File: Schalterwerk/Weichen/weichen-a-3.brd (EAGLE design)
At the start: 100 x 80 mm, 24 parts, among them Q1 P-MOSFET, Q2 P-MOSFET, X1 PHNX_4P_508CONN_1017493, X3 IO-HAT, X4 RJ45-JACK, X5 PHNX_4P_350CONN_1984989_PXC, X6 PHNX_4P_350CONN_1984989_PXC

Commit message: Completes copy-paste of the layout of the conneectors to the schalterwerk.
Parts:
- added H1, H2, H3, H4: MOUNT-HOLE3.3, holes:3,3
- moved X4 222.4 mm to (95.2, 40.0), turned to 90 degrees
- moved X6 173.7 mm to (95.2, 15.2), turned to 90 degrees
- moved X5 144.5 mm to (95.2, 54.6), turned to 90 degrees
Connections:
- net NX41: now also X5.4; no longer X5.1
- net NX42: now also X5.3; no longer X5.2
- net NX43: now also X5.2; no longer X5.3
- net NX44: now also X6.4; no longer X6.1
- net NX45: now also X6.3; no longer X6.2
- net NX46: now also X5.1; no longer X5.4
- net NX47: now also X6.2; no longer X6.3
- net NX48: now also X6.1; no longer X6.4
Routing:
- net NX41: track 0.00 -> 64.1 mm, vias 0 -> 3
- net NX48: track 0.00 -> 56.9 mm, vias 0 -> 1
- net NX47: track 0.00 -> 53.0 mm, vias 0 -> 1
- net NX42: track 0.00 -> 52.3 mm, vias 0 -> 1
- net NX43: track 0.00 -> 49.2 mm, vias 0 -> 3
- net NX45: track 0.00 -> 44.2 mm, vias 0 -> 1
- net NX46: track 0.00 -> 42.3 mm, vias 0 -> 1
- net NX44: track 0.00 -> 37.7 mm, vias 0 -> 1
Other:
- board size 100 x 80 mm -> 100.3 x 80 mm
- board text added: "CH1 schalt"
- board text added: "CH2 schalt"
- board text added: "CH3 schalt"
- board text added: "CH4 schalt"
- board text added: "V+"

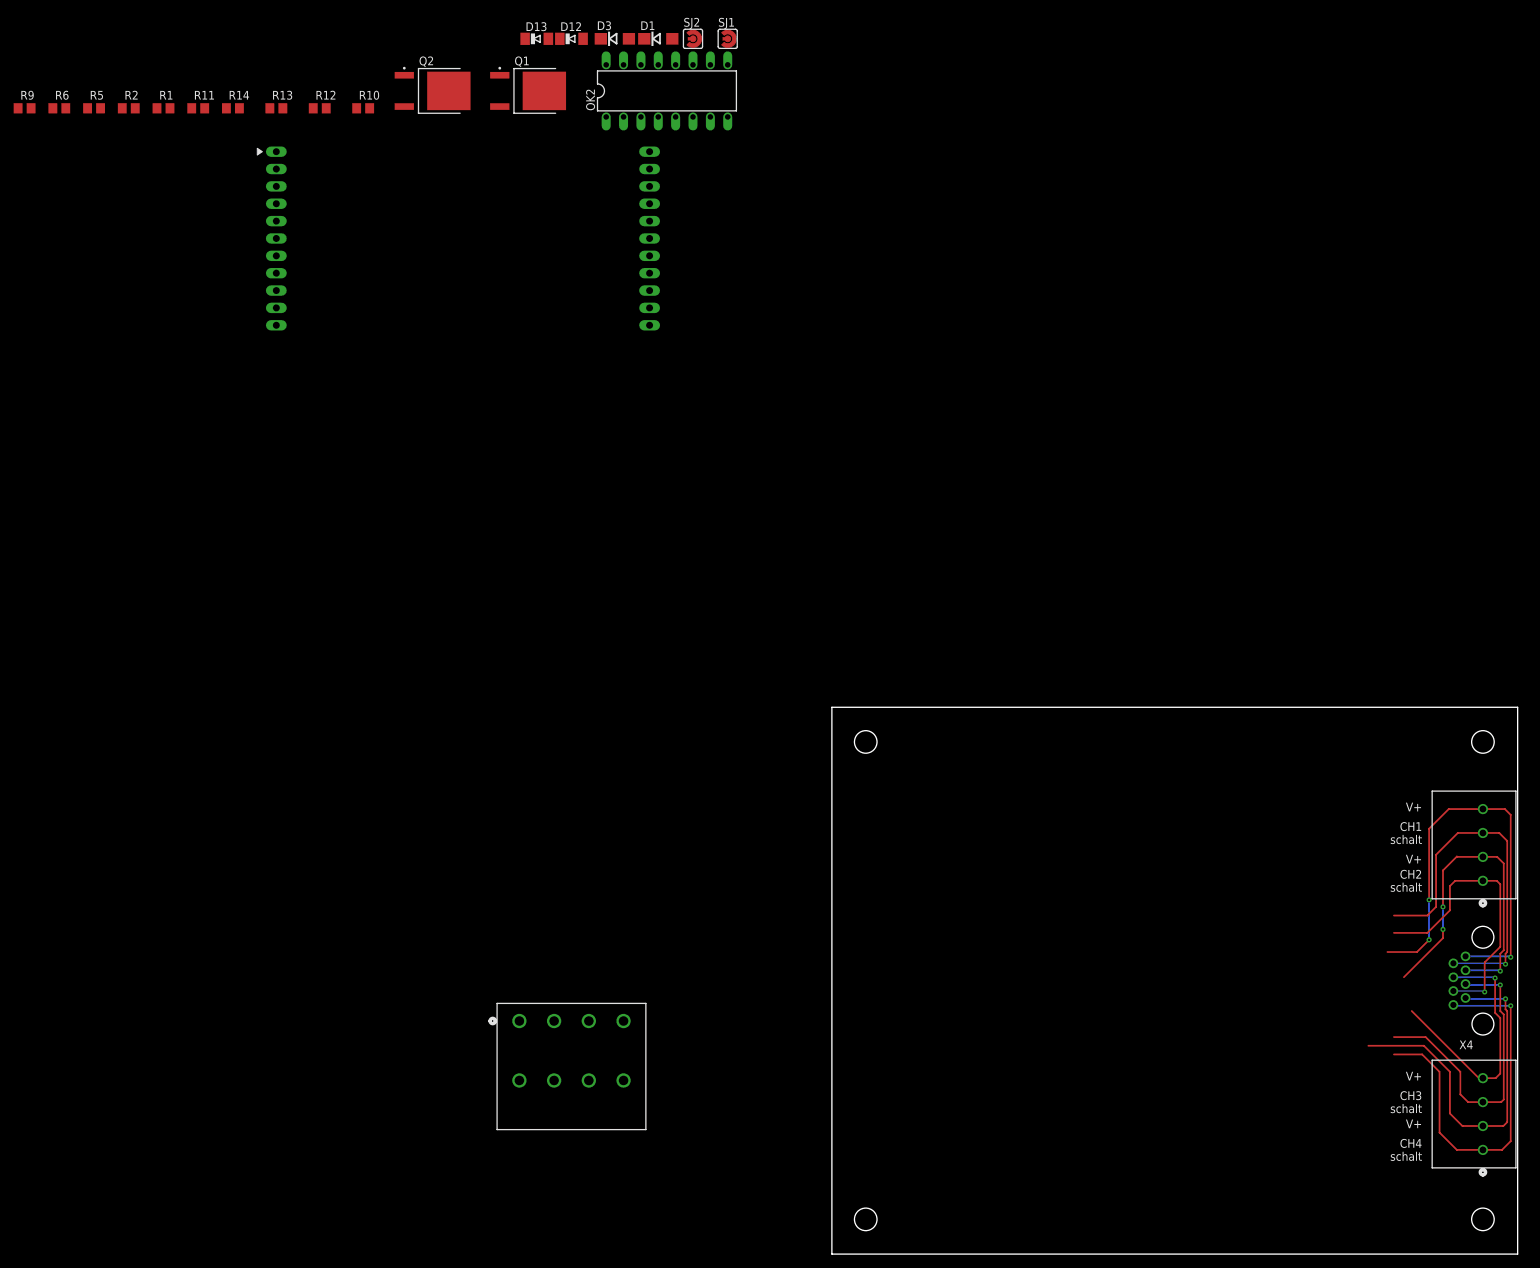
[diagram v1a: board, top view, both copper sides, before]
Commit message: Does much of the board layout. Switches the pins on the connector to the schalterwerk so that it is in the order of L1 .. L4.
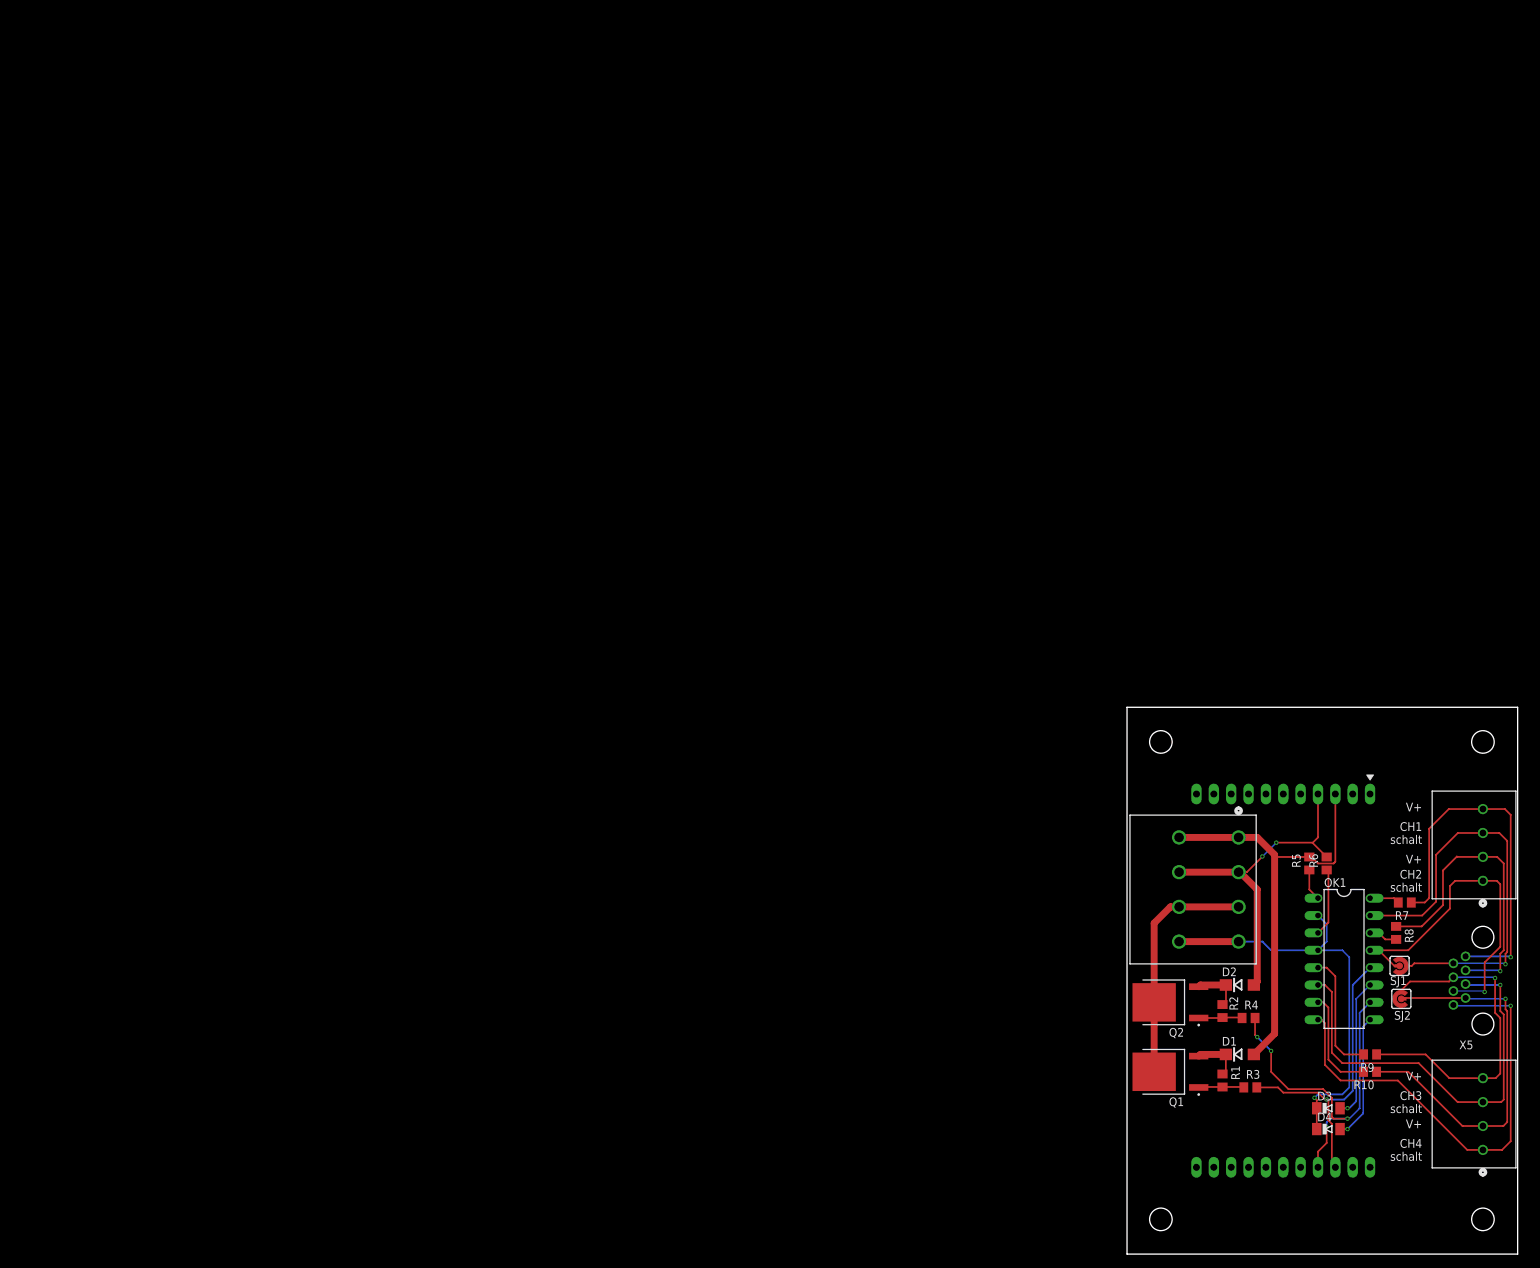
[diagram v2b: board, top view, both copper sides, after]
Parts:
- removed D12, D13: (no value), diode:MINIMELF
- removed OK2: PC847, optocoupler:DIL16
- removed R11, R12: 100, rcl:R0805
- removed R13, R14: 1k5, rcl:R0805
- removed X6: PHNX_4P_350CONN_1984989_PXC, eagleparts:PHNX_4P_350
- added D2: (no value), diode:DO214AC
- added D4: (no value), diode:MINIMELF
- added OK1: PC847, optocoupler:DIL16
- added R3, R4: 5k, rcl:R0805
- added R7, R8: 100, rcl:R0805
- added X2: IO-HAT, eagleparts:IOBOARD
- D3: device diode:DO214AC -> diode:MINIMELF
- R10, R9: value 5k -> 1k5
- X3: value IO-HAT -> PHNX_4P_350CONN_1984989_PXC; device eagleparts:IOBOARD -> eagleparts:PHNX_4P_350
- X4: value RJ45-JACK -> PHNX_4P_350CONN_1984989_PXC; device trainlib:RJ45-PULSE-E5J88 -> eagleparts:PHNX_4P_350
- X5: value PHNX_4P_350CONN_1984989_PXC -> RJ45-JACK; device eagleparts:PHNX_4P_350 -> trainlib:RJ45-PULSE-E5J88
- moved R9 240.7 mm to (78.7, 29.2), turned to 180 degrees
- moved R6 215.8 mm to (72.4, 57.1), turned to 90 degrees
- moved R1 210.3 mm to (57.1, 25.4), turned to 270 degrees
- moved R5 209.3 mm to (69.8, 57.1), turned to 90 degrees
- moved R2 207.5 mm to (57.1, 35.6), turned to 270 degrees
- moved X3 205.0 mm to (95.2, 54.6), turned to 90 degrees
- moved R10 203.9 mm to (78.7, 26.7), turned to 180 degrees
- moved D3 188.1 mm to (72.6, 21.3)
- moved SJ2 174.6 mm to (83.3, 37.3), turned to 180 degrees
- moved Q2 171.6 mm to (49.5, 36.8), turned to 180 degrees
- moved Q1 171.5 mm to (49.5, 26.7), turned to 180 degrees
- moved D1 171.2 mm to (59.7, 29.2)
- moved SJ1 167.5 mm to (83.1, 42.2)
- moved X1 83.8 mm to (50.8, 45.7), turned to 270 degrees
- moved H1 43.2 mm to (48.1, 74.9)
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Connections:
- net +12V: now also X2.P$1; no longer X3.P$1
- net 12V2: now also X2.P$22; no longer X3.P$22
- net GND: now also X2.P$11, X2.P$12, X2.P$2, X2.P$21; no longer X3.P$11, X3.P$12, X3.P$2, X3.P$21
- net L1: now also R5.2, X2.P$3; no longer R9.2, X3.P$3
- net L2: now also D2.A, R6.2, X1.3, X1.4, X2.P$4; no longer D3.A, R10.2, X1.5, X1.6, X3.P$4
- net L3: now also X1.5, X1.6; no longer X1.3, X1.4
- net L4: now also D3.C, D4.C, OK1.2, OK1.4; no longer D12.C, D13.C, OK2.2, OK2.4
- net N$1: now also D2.C; no longer D3.C
- net N$12: now also R4.1; no longer R6.1
- net N$15: now also OK1.12, R3.2, X2.P$20; no longer OK2.12, R5.2, X3.P$20
- net N$16: now also OK1.10, R4.2, X2.P$19; no longer OK2.10, R6.2, X3.P$19
- net N$17: now also D3.A, OK1.11; no longer D12.A, OK2.11
- net N$19: now also OK1.16, R7.2; no longer OK2.16, R11.2
- net N$2: now also OK1.1, R5.1; no longer OK2.1, R9.1
- net N$21: now also OK1.14, R8.2; no longer OK2.14, R12.2
- net N$22: now also D4.A, OK1.9; no longer D13.A, OK2.9
- net N$24: now also X2.P$18; no longer X3.P$18
- net N$25: now also X2.P$17; no longer X3.P$17
- net N$5: now also OK1.5, R9.2; no longer OK2.5, R13.2
- net N$7: now also OK1.3, R6.1; no longer OK2.3, R10.1
- net N$8: now also OK1.7, R10.2; no longer OK2.7, R14.2
- net N$9: now also R3.1; no longer R5.1
- net NX41: now also R7.1, X3.4, X5.1; no longer R11.1, X4.1, X5.4
- net NX42: now also OK1.15, X3.3, X5.2; no longer OK2.15, X4.2, X5.3
- net NX43: now also R8.1, X3.2, X5.3; no longer R12.1, X4.3, X5.2
- net NX44: now also R9.1, X5.4; no longer R13.1, X6.4
- net NX45: now also OK1.6, X4.3, X5.5; no longer OK2.6, X4.5, X6.3
- net NX46: now also OK1.13, X3.1, X5.6; no longer OK2.13, X4.6, X5.1
- net NX47: now also R10.1, X4.2, X5.7; no longer R14.1, X4.7, X6.2
- net NX48: now also OK1.8, X4.1, X5.8; no longer OK2.8, X4.8, X6.1
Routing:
- net L1: track 0.00 -> 64.9 mm
- net L4: track 0.00 -> 61.4 mm, vias 0 -> 1
- net N$16: track 0.00 -> 53.4 mm, vias 0 -> 4
- net L2: track 0.00 -> 49.6 mm, vias 0 -> 2
- net N$15: track 0.00 -> 44.8 mm, vias 0 -> 1
- net L3: track 0.00 -> 35.1 mm
- net N$17: track 0.00 -> 20.6 mm, vias 0 -> 1
- net N$22: track 0.00 -> 18.5 mm, vias 0 -> 1
- net N$5: track 0.00 -> 17.9 mm
- net NX45: track 44.2 -> 61.7 mm
- net N$8: track 0.00 -> 15.3 mm
- net NX44: track 37.7 -> 50.9 mm
- net NX48: track 56.9 -> 68.4 mm
- net NX41: track 64.1 -> 54.0 mm, vias 3 -> 1
- net NX42: track 52.3 -> 62.4 mm
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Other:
- board size 100.3 x 80 mm -> 57.1 x 80 mm

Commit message: Adds all display LEDs, completes layout.
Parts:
- added C1, C2: 500n25V, rcl:C0805
- added D10, D12, D6, D8: LEDHEADER, eagleparts:LEDHEADER
- added D11, D5, D7, D9: (no value), led:CHIPLED_0603
- added R11, R12, R13, R14, R17, R18: 5k, rcl:R0805
- added R15, R16: 10k, rcl:R0805
- moved R1 2.54 mm to (59.7, 25.4)
- moved R2 2.54 mm to (59.7, 35.6)
- moved R4 1.63 mm to (62.2, 35.6), turned to 90 degrees
- moved R3 1.44 mm to (62.2, 25.4), turned to 90 degrees
- moved Q1 0.76 mm to (50.3, 26.7)
- moved Q2 0.76 mm to (50.3, 36.8)
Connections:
- removed net N$15: OK1.12, R3.2, X2.P$20
- removed net N$16: OK1.10, R4.2, X2.P$19
- removed net N$9: Q1.1, R1.2, R3.1
- new net IST1: D10.C, D9.C, OK1.12, R3.2, X2.P$20
- new net IST2: D11.C, D12.C, OK1.10, R4.2, X2.P$19
- new net N$10: D8.A, R12.1
- new net N$11: D9.A, R15.1
- new net N$14: D10.A, R16.1
- new net N$18: D11.A, R17.1
- new net N$20: D12.A, R18.1
- new net N$23: C1.2, Q1.1, R1.2, R3.1
- new net N$3: D7.A, R11.1
- new net N$4: D5.A, R13.1
- new net N$6: D6.A, R14.1
- net L1: now also R13.2, R14.2
- net L2: now also R11.2, R12.2
- net L4: now also D5.C, D6.C, D7.C, D8.C
- net N$1: now also C2.1, R17.2, R18.2
- net N$12: now also C2.2
- net N$13: now also C1.1, R15.2, R16.2
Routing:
- net IST1: track 0.00 -> 92.7 mm, vias 0 -> 4
- net IST2: track 0.00 -> 92.0 mm, vias 0 -> 8
- net L4: track 61.4 -> 131.1 mm, vias 1 -> 2
- net N$1: track 7.26 -> 69.4 mm, vias 0 -> 6
- net L2: track 49.6 -> 111.7 mm
- net N$16: track 53.4 -> 0.00 mm, vias 4 -> 0
- net N$15: track 44.8 -> 0.00 mm, vias 1 -> 0
- net L1: track 64.9 -> 102.9 mm
- net N$13: track 7.14 -> 41.5 mm, vias 0 -> 6
- net N$23: track 0.00 -> 7.93 mm
- net N$9: track 6.65 -> 0.00 mm
- net N$6: track 0.00 -> 5.40 mm
- net N$3: track 0.00 -> 5.32 mm
- net N$4: track 0.00 -> 5.28 mm
- net N$20: track 0.00 -> 5.21 mm
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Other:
- board text added: "(c) Balazs Racz 20230601"
- board text added: "+"
- board text added: "-"
- board text added: "Ist"
- board text added: "Ist+ schalt"
- board text added: "Ist- schalt"
- board text added: "Masse"
- board text added: "Soll"
- board text added: "Soll + RM"
- board text added: "Soll - RM"
- board text removed: "CH1 schalt"
- board text removed: "CH2 schalt"
- board text removed: "CH3 schalt"
- board text removed: "CH4 schalt"

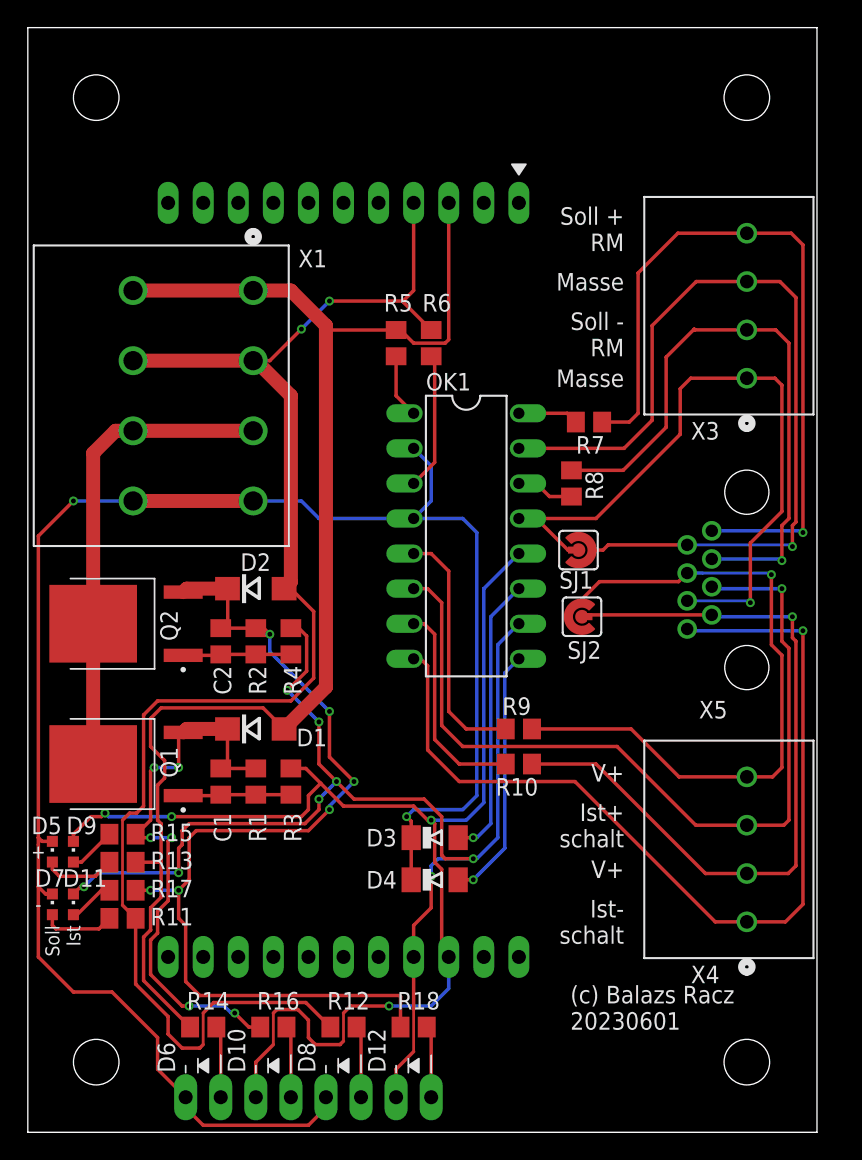
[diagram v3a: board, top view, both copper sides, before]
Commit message: Adds ports to connect adjacent boards. Adds ground pour.
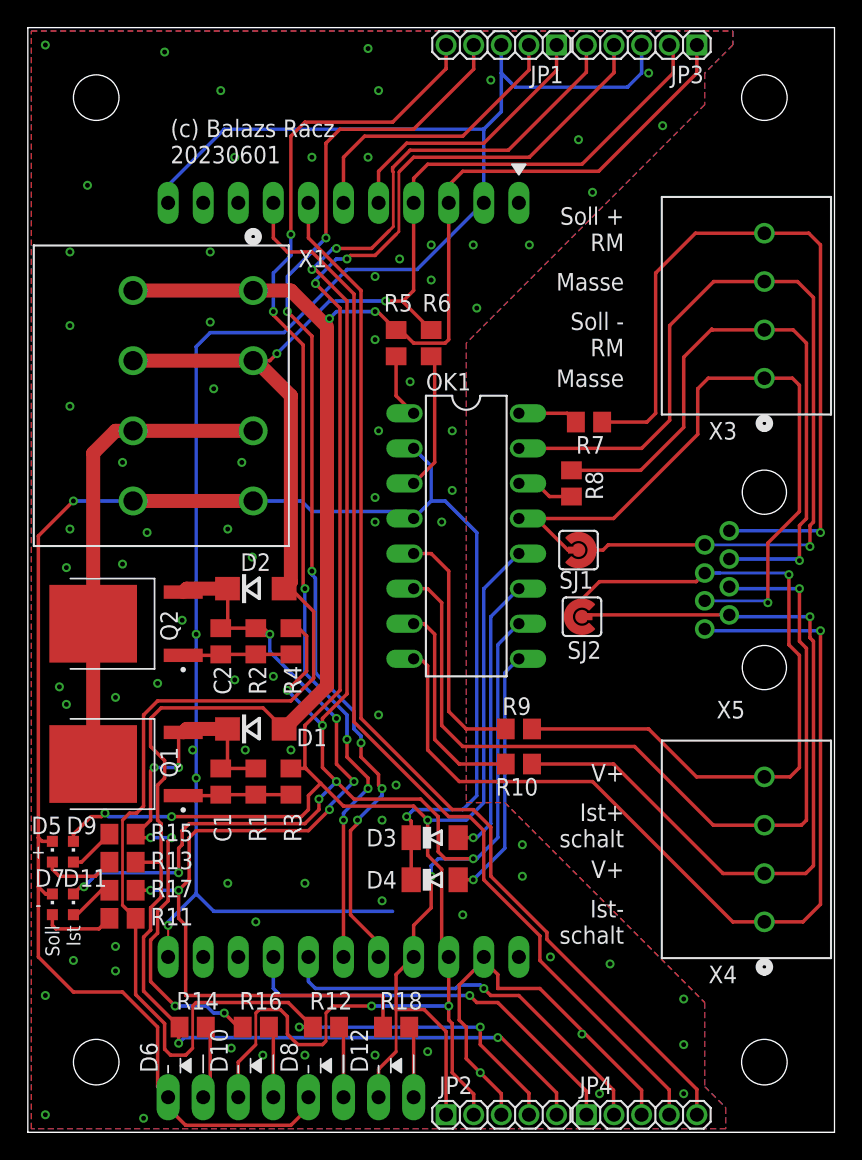
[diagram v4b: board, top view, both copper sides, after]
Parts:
- added JP1, JP2, JP3, JP4: (no value), pinhead:1_05X2MM
- moved D12 1.27 mm to (69.8, 2.54)
- moved D8 1.27 mm to (64.8, 2.54)
- moved R12 1.27 mm to (64.8, 7.62)
- moved R18 1.27 mm to (69.8, 7.62)
- moved D10 1.27 mm to (59.7, 2.54)
- moved D6 1.27 mm to (54.6, 2.54)
- moved R16 1.27 mm to (59.7, 7.62)
- moved H3 1.27 mm to (96.5, 5.08)
- moved H4 1.27 mm to (96.5, 74.9)
- moved X3 1.27 mm to (96.5, 54.6)
- moved X4 1.27 mm to (96.5, 15.2)
- moved X5 1.27 mm to (96.5, 40.0)
- moved R14 0.76 mm to (55.1, 7.62)
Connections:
- removed net N$24: X2.P$18
- removed net N$25: X2.P$17
- new net IN2: JP1.1, X2.P$5
- new net IN3: JP1.2, X2.P$6
- new net IN4: JP4.5, X2.P$7
- new net IN5: JP4.4, X2.P$8
- new net OUT2: JP1.4, X2.P$18
- new net OUT3: JP1.5, X2.P$17
- new net OUT4: JP4.2, X2.P$16
- new net OUT5: JP4.1, X2.P$15
- net GND: now also JP1.3, JP2.3, JP3.3, JP4.3
- net IST1: now also JP2.2, JP3.4
- net IST2: now also JP2.1, JP3.5
- net L1: now also JP2.5, JP3.1
- net L2: now also JP2.4, JP3.2
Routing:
- net GND: track 0.00 -> 166.9 mm, vias 0 -> 85
- net IST1: track 92.7 -> 173.0 mm, vias 4 -> 7
- net IN5: track 0.00 -> 79.8 mm
- net OUT2: track 0.00 -> 79.4 mm, vias 0 -> 6
- net IN4: track 0.00 -> 78.6 mm
- net OUT3: track 0.00 -> 78.5 mm, vias 0 -> 6
- net IST2: track 92.0 -> 168.0 mm, vias 8 -> 10
- net L1: track 102.9 -> 160.6 mm, vias 0 -> 4
- net L2: track 111.7 -> 159.9 mm, vias 2 -> 4
- net OUT5: track 0.00 -> 29.7 mm, vias 0 -> 1
- net OUT4: track 0.00 -> 29.1 mm, vias 0 -> 1
- net IN3: track 0.00 -> 21.2 mm
- net IN2: track 0.00 -> 20.0 mm
- net NX47: track 55.9 -> 58.4 mm
- net NX44: track 50.9 -> 53.5 mm
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- added copper zone on layer 1, net GND
- added copper zone on layer 16, net GND
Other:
- board size 57.1 x 80 mm -> 58.4 x 80 mm
